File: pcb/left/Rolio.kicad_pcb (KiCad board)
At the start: 2 copper layers, 141.8 x 83.9 mm, 110 parts, among them Q1 AO3400A, SW4 SW_DIP_x01

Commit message: Check in V1.0
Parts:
- moved SW4 0.86 mm to (166.6, 40.7)
- moved BATT1 0.81 mm to (166.2, 47.5)
- moved C1 0.81 mm to (179.3, 87.3)
- moved D19 0.81 mm to (179.3, 91.0)
- moved NICE_NANO1 0.81 mm to (174.5, 40.2)
- moved Nice!View1 0.81 mm to (187.2, 73.3)
- moved RESET1 0.81 mm to (169.7, 49.6)
- moved RE_1 0.81 mm to (182.2, 86.2)
- moved C2 0.81 mm to (179.3, 83.9)
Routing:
- net col0: track 230.1 -> 224.2 mm
- net ENC_A: track 57.7 -> 53.7 mm
- net VBATT: track 26.9 -> 30.4 mm, vias 0 -> 2
- net ENC_B: track 50.3 -> 47.8 mm
- net col1: track 215.1 -> 217.3 mm
- net BL_CTRL: track 150.4 -> 151.7 mm
- net BL_GND: track 505.1 -> 506.4 mm
- net MOSI: track 27.5 -> 26.3 mm
- net CS: track 56.1 -> 54.9 mm
- net row3: track 144.4 -> 143.3 mm
- net col3: track 145.1 -> 144.1 mm
- net col5: track 106.0 -> 105.1 mm
- net col4: track 120.8 -> 120.0 mm
- net VCC: track 590.0 -> 589.3 mm
- net row0: track 145.2 -> 145.7 mm
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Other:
- board size 141.8 x 83.9 mm -> 141.5 x 83 mm
- board text added: "Rolio V1.2 (Left) - MickiusMousius '23"
- board text removed: "Rolio V1.01 (Left) - MickiusMousius '23"

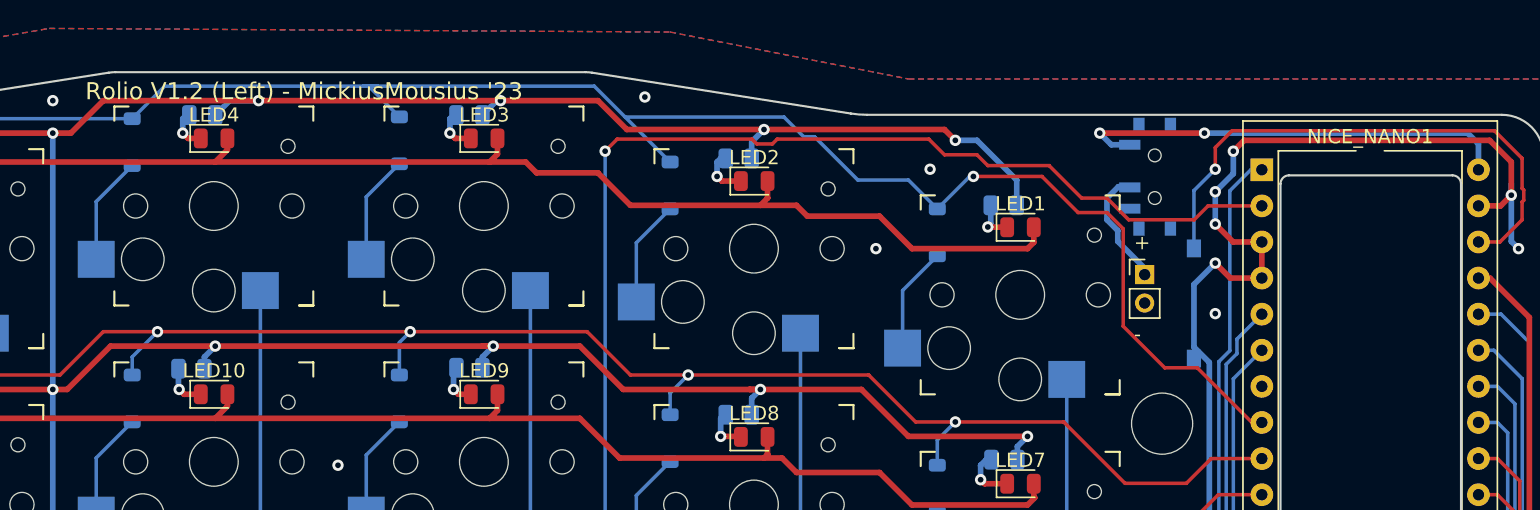
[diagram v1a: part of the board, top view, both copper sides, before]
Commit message: Update PCB to have nicer soldering pads for the battery
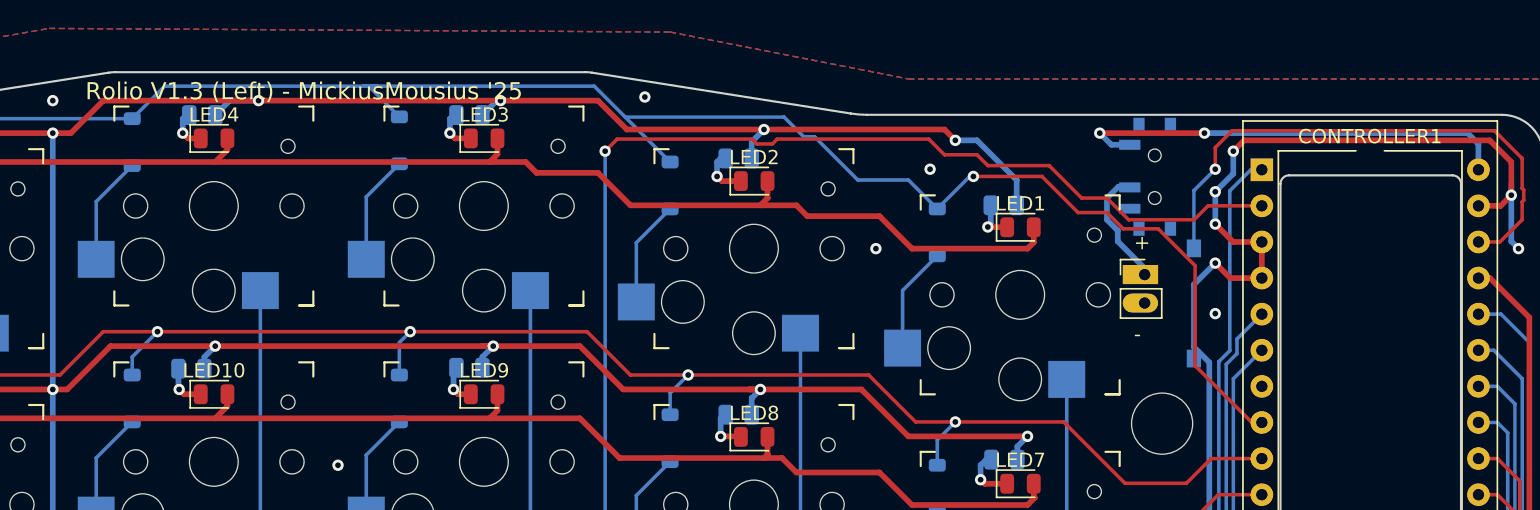
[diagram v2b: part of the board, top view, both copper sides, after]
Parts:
- renumbered NICE_NANO1 to CONTROLLER1
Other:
- board text added: "Rolio V1.3 (Left) - MickiusMousius '25"
- board text removed: "Rolio V1.2 (Left) - MickiusMousius '23"
